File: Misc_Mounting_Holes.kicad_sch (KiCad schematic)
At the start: 12 parts

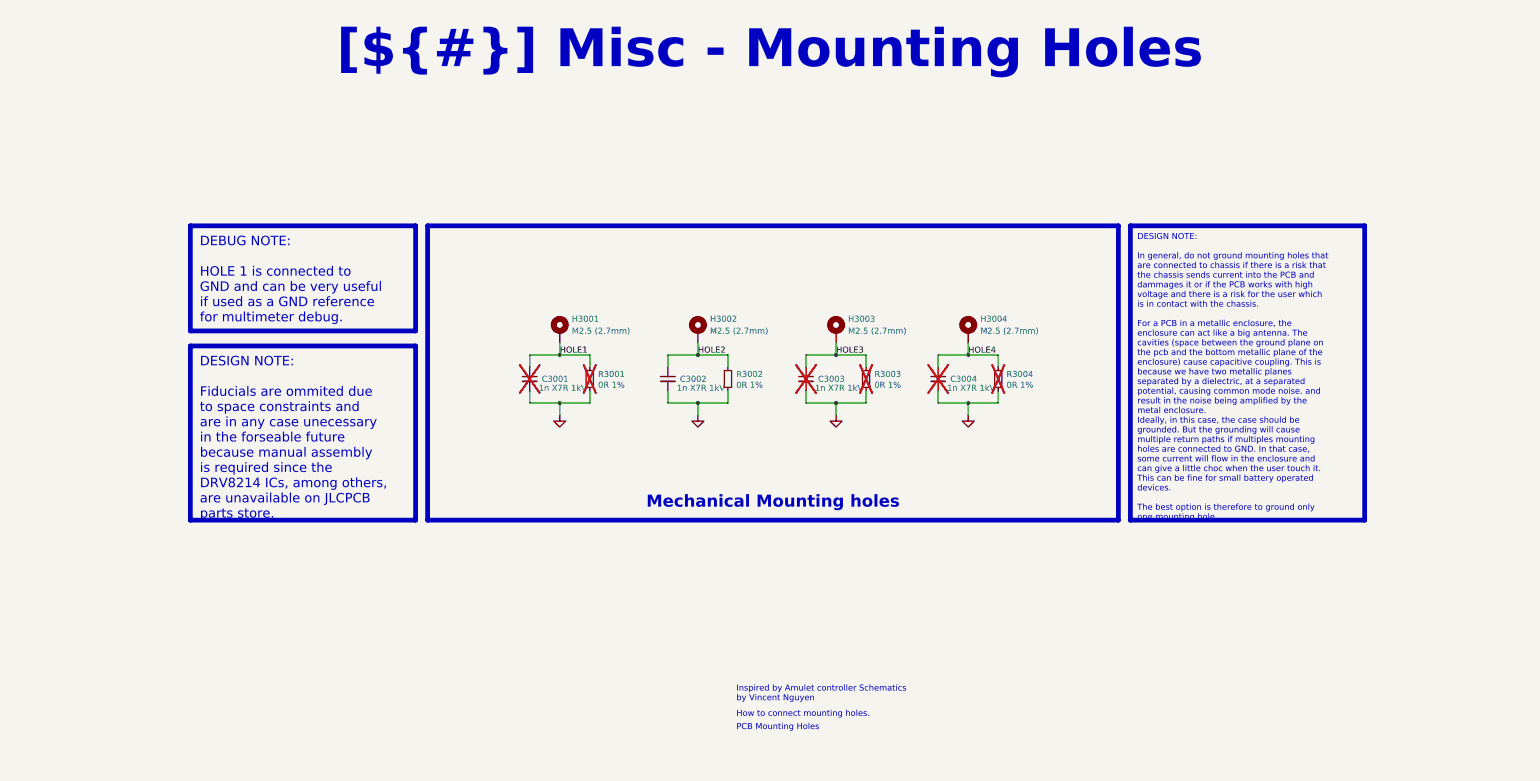
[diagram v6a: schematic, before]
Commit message: Added PCB frame
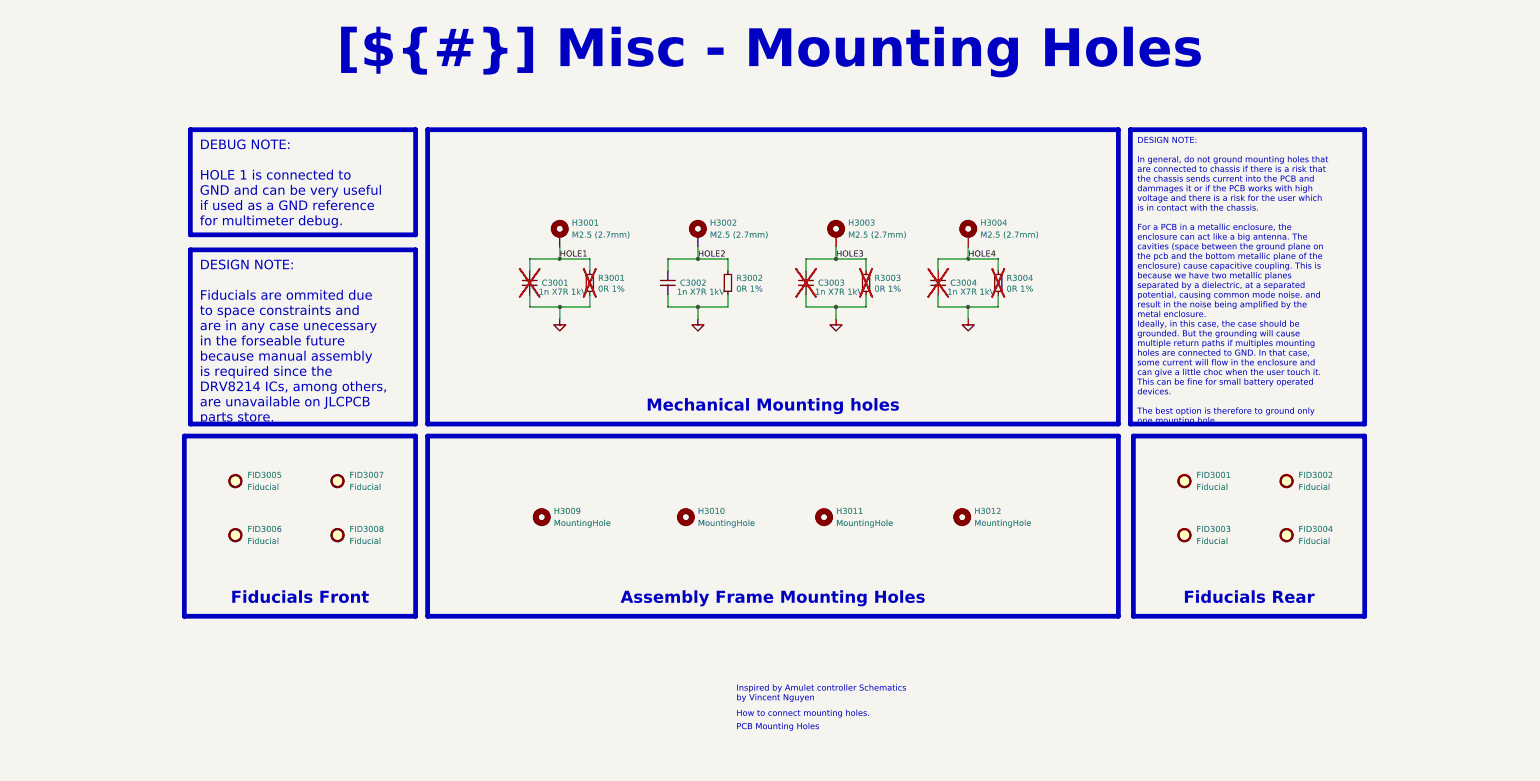
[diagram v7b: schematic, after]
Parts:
- added FID3001, FID3002, FID3003, FID3004, FID3005, FID3006, FID3007, FID3008: Fiducial, Fiducial:Fiducial_0.75mm_Mask2.25mm, symbol Mechanical:Fiducial
- added H3009, H3010, H3011, H3012: MountingHole, MountingHole:MountingHole_3.2mm_M3, symbol Mechanical:MountingHole
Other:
- moved on the sheet: C3001, C3002, C3003, C3004, H3001, H3002, H3003, H3004, R3001, R3002, R3003, R3004

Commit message: Added PCB frame for assembly, almost finished auto-review, only MCU and motors left
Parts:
- renumbered FID3005 to FID3001, FID3007 to FID3002, FID3001 to FID3003, FID3002 to FID3004, FID3006 to FID3005, FID3008 to FID3006, FID3003 to FID3007, FID3004 to FID3008, H3009 to H3005, H3010 to H3006, H3011 to H3007, H3012 to H3008
